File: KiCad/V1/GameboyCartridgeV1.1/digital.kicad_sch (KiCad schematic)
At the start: 29 parts, among them J1 USB_C_Receptacle_USB2.0, J2 DBG_UART, J3 Conn_01x06, SW1 SW_Push, U2 W25Q128JVS, U3 RP2040, Y1 12MHz

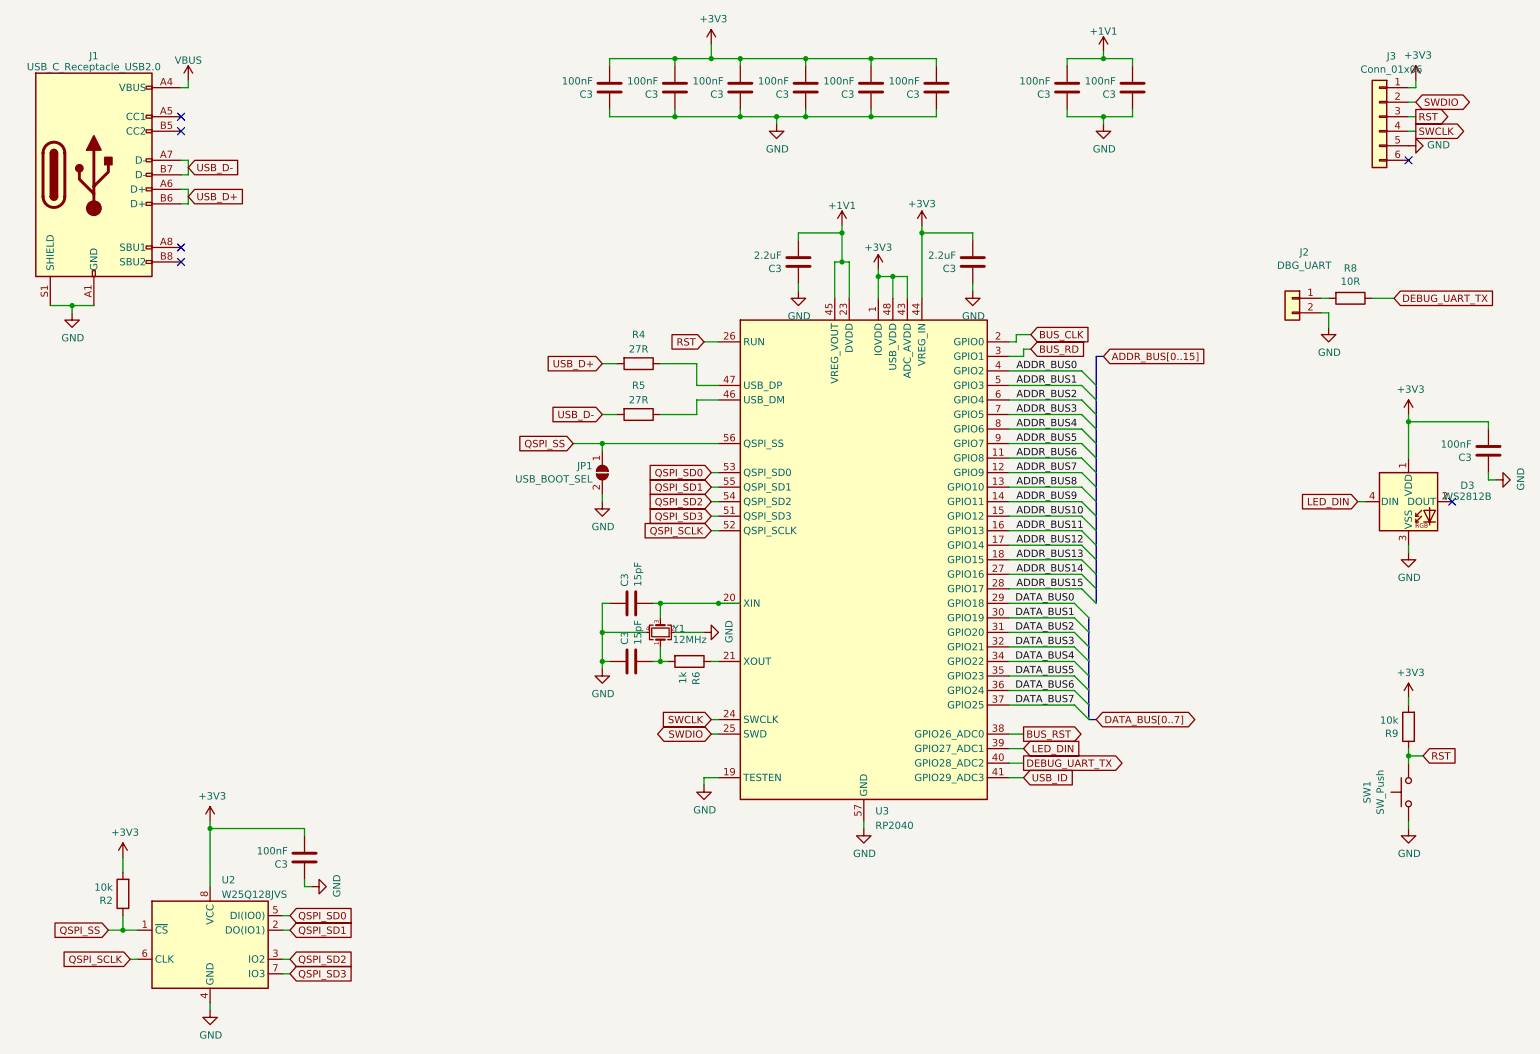
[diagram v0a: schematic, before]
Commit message: Change folder structure
- Fix Library paths
- Add Libraries
- Add Gerbers, BOM, Position file compatible with JLPCB
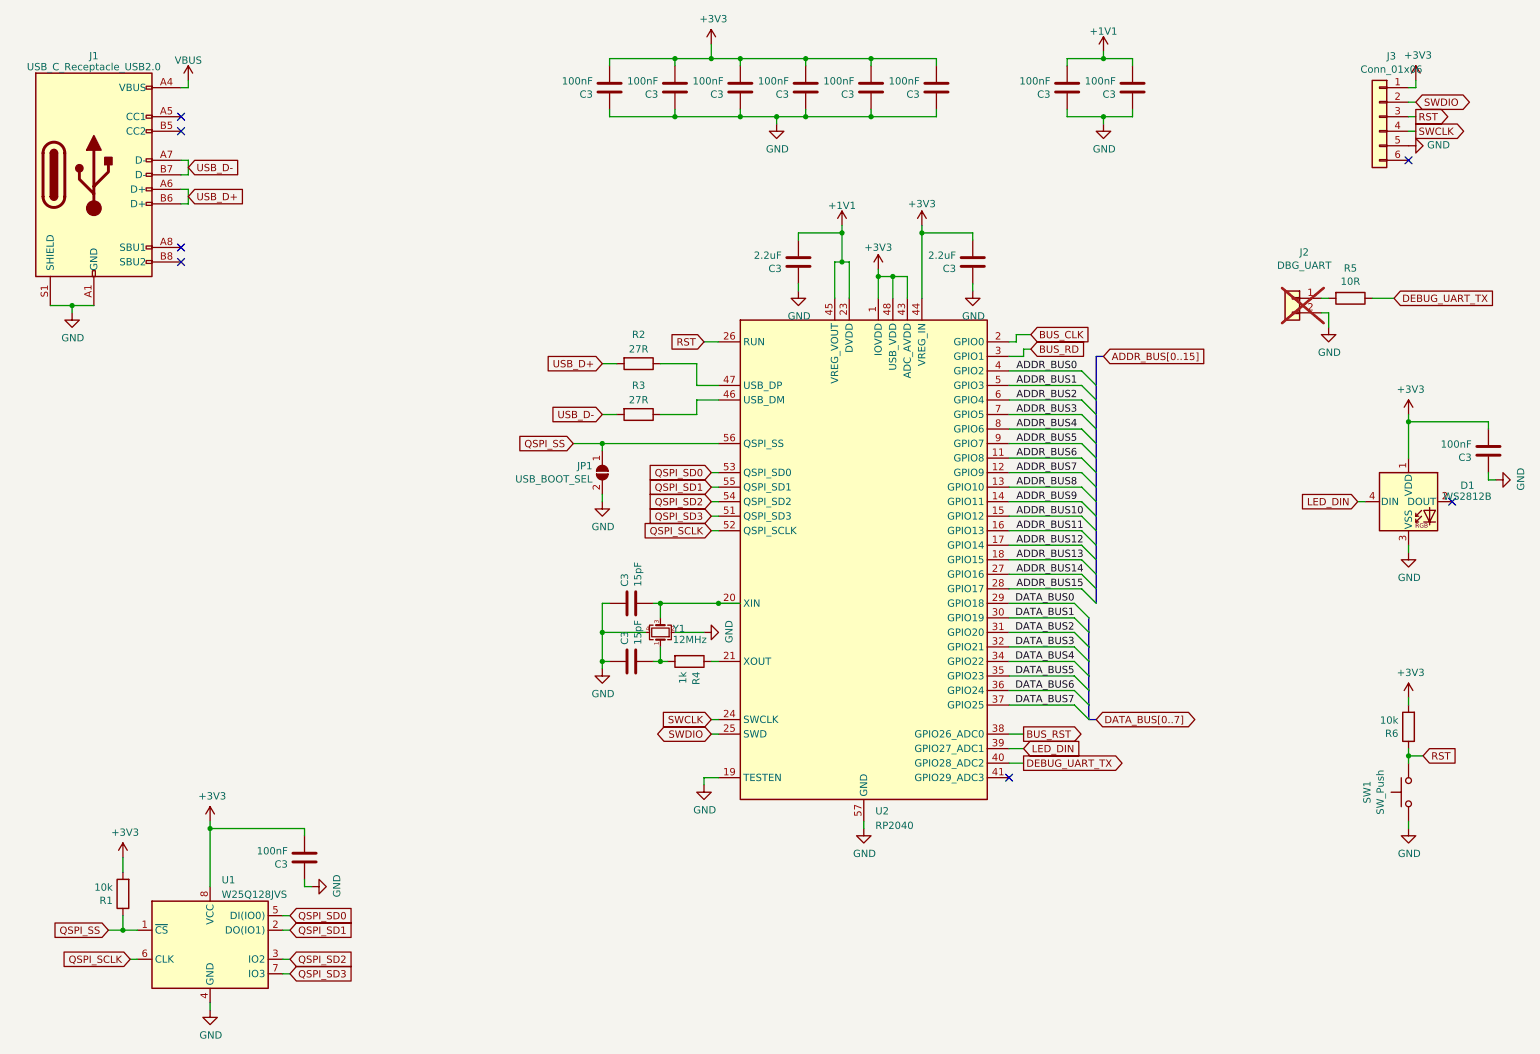
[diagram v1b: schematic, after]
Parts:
- C3: LCSC (none) -> C1644
- D1: renamed from D3; footprint LED_SMD:LED_SK6812MINI_PLCC4_3.5x3.5mm_P1.75mm -> LED_SMD:LED_WS2812B_PLCC4_5.0x5.0mm_P3.2mm; LCSC (none) -> C2761795
- J1: LCSC (none) -> C2927037
- J2: now not fitted; now left out of the parts list
- J3, JP1: now left out of the parts list
- SW1: footprint Button_Switch_SMD:SW_SPST_PTS810 -> Button_Switch_SMD:SW_SPST_TL3342; LCSC (none) -> C2886898
- U1: renamed from U2; LCSC (none) -> C97521
- U2: renamed from U3; LCSC (none) -> C2040
- Y1: LCSC (none) -> C668845
- renumbered R2 to R1, R4 to R2, R5 to R3, R6 to R4, R8 to R5, R9 to R6
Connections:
- net USB_ID: no longer names the net of U2.41 (GPIO29_ADC3)
- no-connect marks 6 -> 7
